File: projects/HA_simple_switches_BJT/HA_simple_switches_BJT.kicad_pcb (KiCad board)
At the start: 2 copper layers, 32.4 x 31.1 mm, 15 parts, among them J1 TerminalBlock_2pin, J2 TerminalBlock_3pin, J3 TerminalBlock_3pin, J4 TerminalBlock_3pin, J5 TerminalBlock_3pin, Q1 MMBT3904, Q2 MMBT3904, Q3 MMBT3904, T1 HA_simple_switches_BJT, T2 (C)UweHerting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

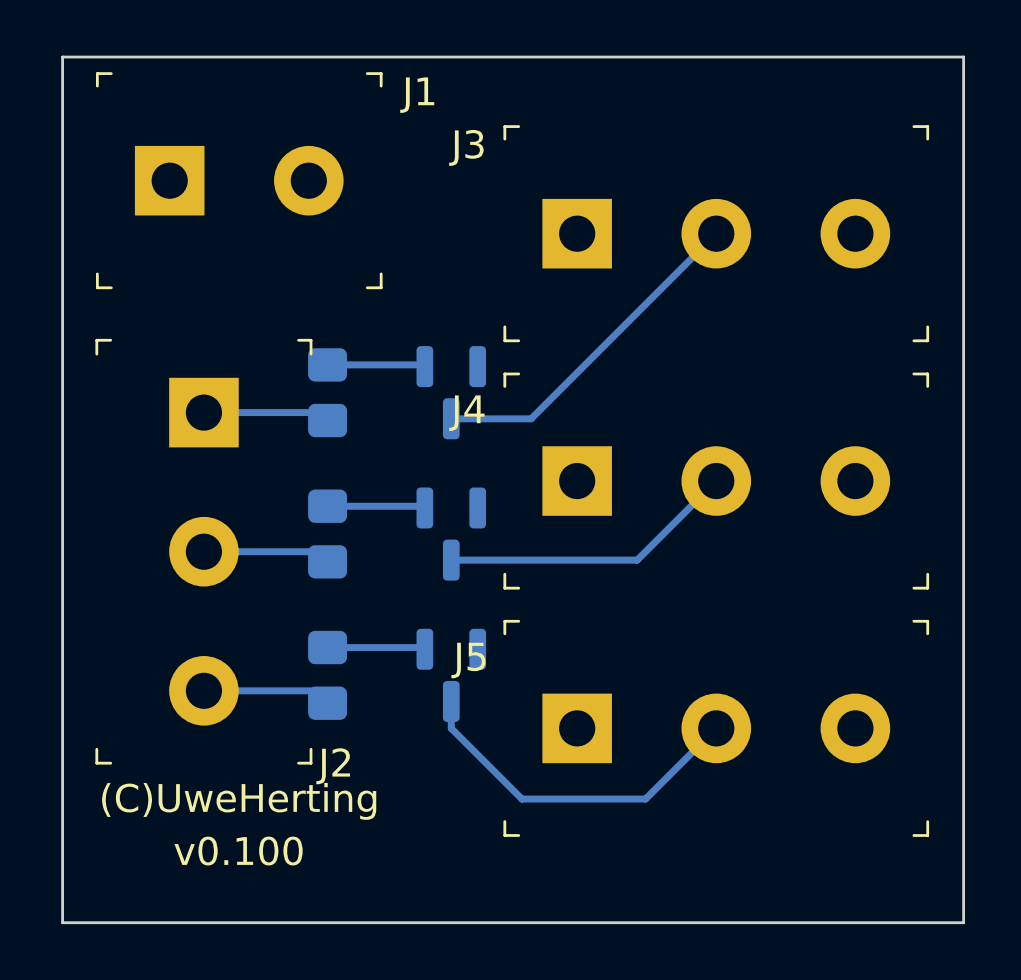
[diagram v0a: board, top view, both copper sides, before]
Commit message: v101 minor routing changes
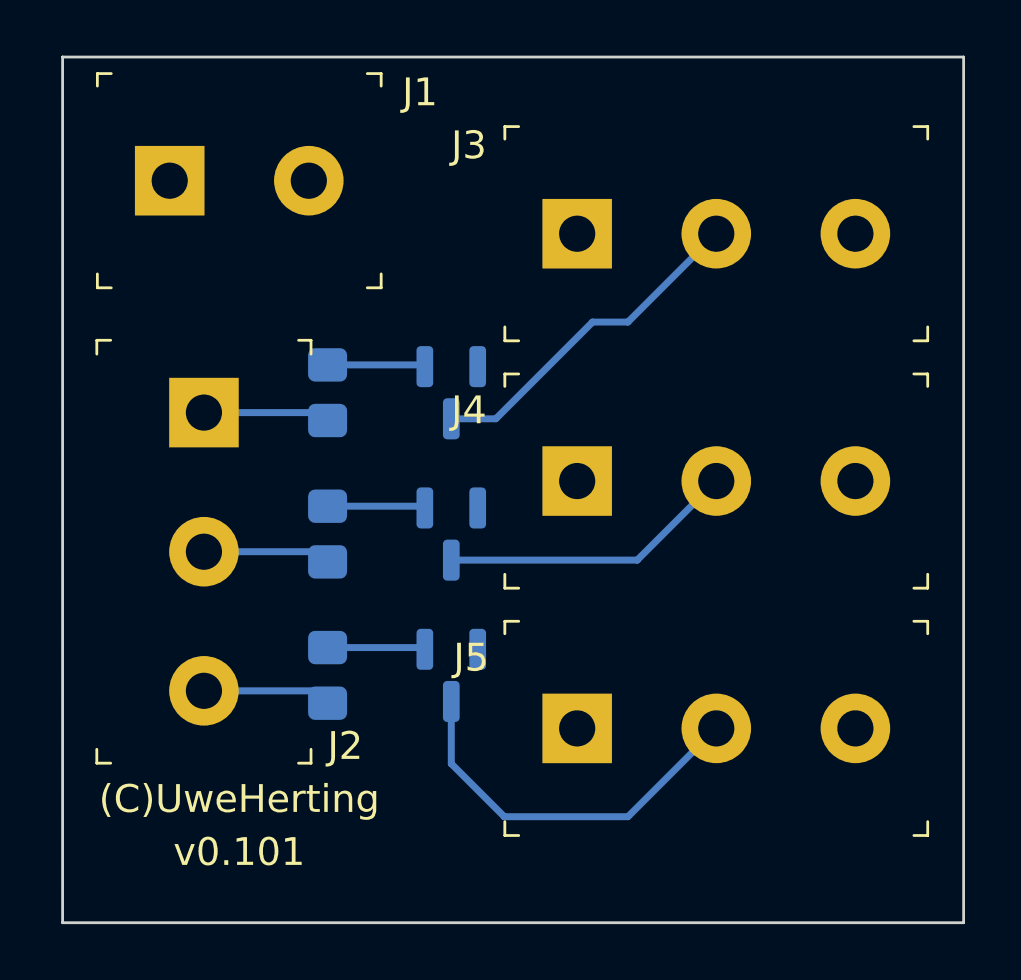
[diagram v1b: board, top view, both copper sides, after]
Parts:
- T4: value v0.100 -> v0.101
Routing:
- net BJT_03: track 12.6 -> 13.9 mm
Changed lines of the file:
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@@
         (effects (font (size 1 1) (thickness 0.15)))
     )
-    (fp_text value "v0.100" (at 0 -0.635 unlocked) (layer "F.SilkS")
+    (fp_text value "v0.101" (at 0 -0.635 unlocked) (layer "F.SilkS")
         (effects (font (size 1 1) (thickness 0.15)))
     )
@@
     (property "ki_keywords" "ED2601-ND OSTTC")
     (attr through_hole)
-    (fp_text reference "J2" (at 12.62 -4.75) (layer "F.SilkS")
+    (fp_text reference "J2" (at 11.985 -5.08) (layer "F.SilkS")
         (effects (font (size 1 1) (thickness 0.15)))
     )
@@
   (segment (start 146.24 108.505) (end 146.685 108.95) (width 0.25) (layer "B.Cu") (net 5))
   (segment (start 142.24 108.505) (end 146.24 108.505) (width 0.25) (layer "B.Cu") (net 5))
-  (segment (start 154.0025 98.7275) (end 160.655 92.075) (width 0.25) (layer "B.Cu") (net 6))
-  (segment (start 151.13 98.7275) (end 154.0025 98.7275) (width 0.25) (layer "B.Cu") (net 6))
+  (segment (start 156.21 95.25) (end 157.48 95.25) (width 0.25) (layer "B.Cu") (net 6))
+  (segment (start 151.13 98.7275) (end 152.7325 98.7275) (width 0.25) (layer "B.Cu") (net 6))
+  (segment (start 157.48 95.25) (end 160.655 92.075) (width 0.25) (layer "B.Cu") (net 6))
+  (segment (start 152.7325 98.7275) (end 156.21 95.25) (width 0.25) (layer "B.Cu") (net 6))
   (segment (start 151.13 103.8075) (end 157.8125 103.8075) (width 0.25) (layer "B.Cu") (net 7))
   (segment (start 157.8125 103.8075) (end 160.655 100.965) (width 0.25) (layer "B.Cu") (net 7))
-  (segment (start 153.67 112.395) (end 158.115 112.395) (width 0.25) (layer "B.Cu") (net 8))
-  (segment (start 151.13 109.855) (end 153.67 112.395) (width 0.25) (layer "B.Cu") (net 8))
-  (segment (start 151.13 108.8875) (end 151.13 109.855) (width 0.25) (layer "B.Cu") (net 8))
-  (segment (start 158.115 112.395) (end 160.655 109.855) (width 0.25) (layer "B.Cu") (net 8))
+  (segment (start 153.035 113.03) (end 157.48 113.03) (width 0.25) (layer "B.Cu") (net 8))
+  (segment (start 151.13 111.125) (end 153.035 113.03) (width 0.25) (layer "B.Cu") (net 8))
+  (segment (start 157.48 113.03) (end 160.655 109.855) (width 0.25) (layer "B.Cu") (net 8))
+  (segment (start 151.13 108.8875) (end 151.13 111.125) (width 0.25) (layer "B.Cu") (net 8))
   (segment (start 150.1175 96.79) (end 150.18 96.8525) (width 0.25) (layer "B.Cu") (net 9))
   (segment (start 146.685 96.79) (end 150.1175 96.79) (width 0.25) (layer "B.Cu") (net 9))

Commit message: snapshot
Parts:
- removed T2: (C)UweHerting, UH_HA:Copyright-Uwe_Herting
- removed T3: github.com/uherting/MyKiCADRep, UH_HA:GithubLink_UH
- J1: value TerminalBlock_2pin -> Conn_01x02_Pin; footprint UH_HA:Term_Block_1x2_P5mm -> Connector_PinHeader_2.54mm:PinHeader_1x02_P2.54mm_Vertical
- J2, J3, J4, J5: value TerminalBlock_3pin -> Conn_01x03_Pin; footprint UH_HA:Term_Block_1x3_P5mm -> Connector_PinHeader_2.54mm:PinHeader_1x03_P2.54mm_Vertical
- T1: moved to F.Cu
- T4: value v0.101 -> v0.102
- moved T1 14.8 mm to (156.8, 102.2), turned to 0 degrees
- moved J3 14.0 mm to (156.2, 106.0)
- moved T4 12.2 mm to (149.2, 104.1)
- moved J1 11.4 mm to (140.3, 101.6), turned to 90 degrees
- moved J5 10.2 mm to (165.1, 106.0)
- moved R1 9.51 mm to (146.7, 107.3), turned to 0 degrees
- moved Q1 8.88 mm to (151.1, 106.7), turned to 0 degrees
- moved R2 8.24 mm to (146.7, 111.1), turned to 0 degrees
- moved J2 7.75 mm to (140.3, 106.0), turned to 0 degrees
- moved Q2 7.60 mm to (151.1, 110.5), turned to 0 degrees
- moved J4 7.12 mm to (160.7, 106.0)
- moved R3 6.97 mm to (146.7, 114.9), turned to 0 degrees
- moved Q3 6.33 mm to (151.1, 114.3), turned to 0 degrees
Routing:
- net BJT_01: track 12.3 -> 5.30 mm, vias 0 -> 1
- net BJT_03: track 13.9 -> 16.5 mm, vias 0 -> 1
- net GPIO_3: track 4.63 -> 6.93 mm
- net GPIO_2: track 4.60 -> 6.41 mm
- net BJT_02: track 10.7 -> 12.4 mm, vias 0 -> 1
- net GPIO_1: track 4.56 -> 5.88 mm
- net Net-(Q3-B): track 3.52 -> 2.64 mm
- net Net-(Q2-B): track 3.52 -> 2.64 mm
- net Net-(Q1-B): track 3.52 -> 2.64 mm
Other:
- board size 32.4 x 31.1 mm -> 31.1 x 17.8 mm
